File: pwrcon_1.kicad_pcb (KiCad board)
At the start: 2 copper layers, 98.3 x 58.4 mm, 36 parts, among them J1 Conn_01x02, J4 CON3, J5 Conn_01x03_Female, J6 Conn_02x04_Odd_Even, J7 Conn_01x03_Female, Q1 Q_PNP_BCE, U1 LM358

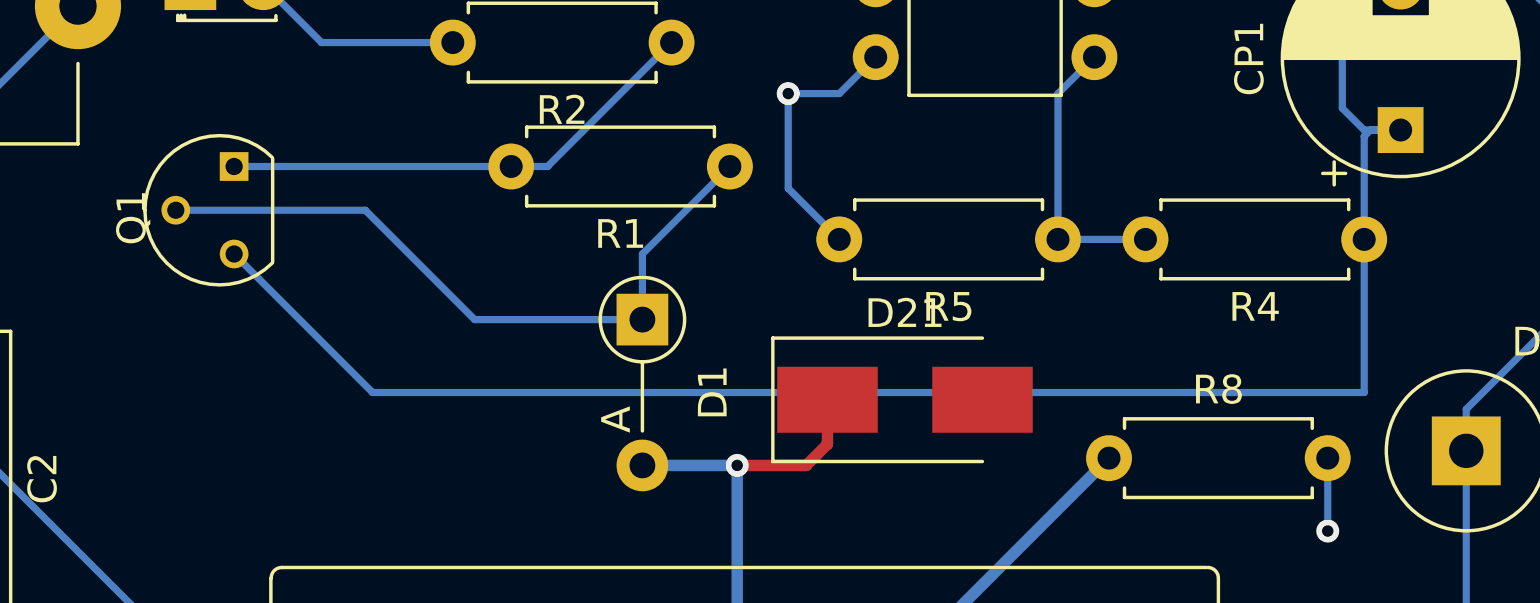
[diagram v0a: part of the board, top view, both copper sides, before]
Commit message: Changed pcb file for transistor flip in previous commit. Changed PSU module name in schematic
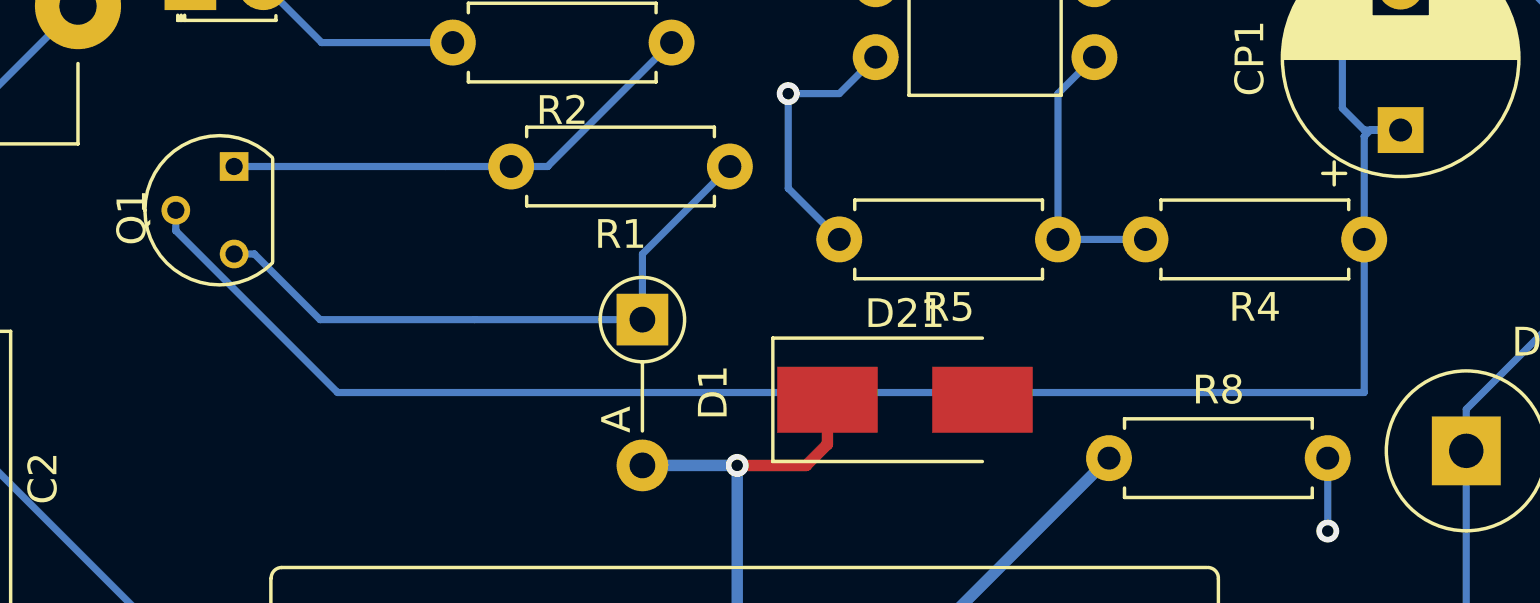
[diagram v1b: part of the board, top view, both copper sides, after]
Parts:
- PSU1: value PD05-20BXX -> IRM-01-3.3
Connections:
- Q1 pad 2: Net-(D1-Pad1) -> Net-(CP1-Pad1)
- Q1 pad 3: Net-(CP1-Pad1) -> Net-(D1-Pad1)
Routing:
- net Net-(CP1-Pad1): track 68.6 -> 71.7 mm
- net Net-(D1-Pad1): track 24.4 -> 21.8 mm
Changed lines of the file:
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@@
-(kicad_pcb (version 20171130) (host pcbnew 5.1.2-f72e74a~84~ubuntu18.04.1)
+(kicad_pcb (version 20171130) (host pcbnew 5.1.5-52549c5~84~ubuntu18.04.1)
   (general
     (thickness 1.6)
     (drawings 8)
-    (tracks 152)
+    (tracks 155)
     (zones 0)
     (modules 36)
@@
   )
   (setup
-    (last_trace_width 0.4)
+    (last_trace_width 0.25)
     (user_trace_width 0.4)
     (user_trace_width 0.5)
@@
       (effects (font (size 1 1) (thickness 0.15)))
     )
-    (fp_text value PD05-20BXX (at -10.16 8.39) (layer F.Fab)
+    (fp_text value IRM-01-3.3 (at -10.16 8.39) (layer F.Fab)
       (effects (font (size 1 1) (thickness 0.15)))
     )
@@
     )
     (pad 3 thru_hole circle (at 0 0 180) (size 1 1) (drill 0.6) (layers *.Cu *.Mask)
-      (net 11 "Net-(CP1-Pad1)"))
+      (net 9 "Net-(D1-Pad1)"))
     (pad 1 thru_hole rect (at 3.048 0 180) (size 1 1) (drill 0.6) (layers *.Cu *.Mask)
       (net 8 "Net-(Q1-Pad1)"))
     (pad 2 thru_hole circle (at 1.524 -2.032 180) (size 1 1) (drill 0.6) (layers *.Cu *.Mask)
-      (net 9 "Net-(D1-Pad1)"))
+      (net 11 "Net-(CP1-Pad1)"))
     (model ${KISYS3DMOD}/TO_SOT_Packages_THT.3dshapes/TO-92_Molded_Narrow.wrl
       (offset (xyz 1.269999980926514 0 0))
@@
   (segment (start 157.48 81.026) (end 161.798 76.708) (width 0.25) (layer B.Cu) (net 8))
   (segment (start 156.21 81.026) (end 157.48 81.026) (width 0.25) (layer B.Cu) (net 8))
-  (segment (start 144.526 82.55) (end 151.13 82.55) (width 0.25) (layer B.Cu) (net 9))
   (segment (start 154.94 86.36) (end 160.782 86.36) (width 0.25) (layer B.Cu) (net 9))
-  (segment (start 151.13 82.55) (end 154.94 86.36) (width 0.25) (layer B.Cu) (net 9))
   (segment (start 160.782 84.074) (end 163.83 81.026) (width 0.25) (layer B.Cu) (net 9))
   (segment (start 160.782 86.36) (end 160.782 84.074) (width 0.25) (layer B.Cu) (net 9))
+  (segment (start 149.551106 86.36) (end 154.94 86.36) (width 0.25) (layer B.Cu) (net 9))
+  (segment (start 147.265106 84.074) (end 149.551106 86.36) (width 0.25) (layer B.Cu) (net 9))
+  (segment (start 146.558 84.074) (end 147.265106 84.074) (width 0.25) (layer B.Cu) (net 9))
   (segment (start 149.606 76.708) (end 154.178 76.708) (width 0.25) (layer B.Cu) (net 10))
   (segment (start 147.574 74.676) (end 149.606 76.708) (width 0.25) (layer B.Cu) (net 10))
@@
   (segment (start 177.329999 70.395999) (end 180.123999 70.395999) (width 0.25) (layer B.Cu) (net 11))
   (segment (start 176.53 69.596) (end 177.329999 70.395999) (width 0.25) (layer B.Cu) (net 11))
-  (segment (start 185.928 88.9) (end 185.928 83.566) (width 0.25) (layer B.Cu) (net 11))
-  (segment (start 146.558 84.074) (end 151.384 88.9) (width 0.25) (layer B.Cu) (net 11))
-  (segment (start 151.384 88.9) (end 185.928 88.9) (width 0.25) (layer B.Cu) (net 11))
+  (segment (start 144.526 83.257106) (end 144.526 82.55) (width 0.25) (layer B.Cu) (net 11))
+  (segment (start 185.928 88.9) (end 150.162998 88.9) (width 0.25) (layer B.Cu) (net 11))
+  (segment (start 144.526 83.263002) (end 144.526 83.257106) (width 0.25) (layer B.Cu) (net 11))
+  (segment (start 150.162998 88.9) (end 144.526 83.263002) (width 0.25) (layer B.Cu) (net 11))
+  (segment (start 185.928 83.566) (end 185.928 88.9) (width 0.25) (layer B.Cu) (net 11))
   (segment (start 181.61 65.278) (end 180.34 65.278) (width 0.25) (layer B.Cu) (net 12))
   (segment (start 184.658 68.326) (end 181.61 65.278) (width 0.25) (layer B.Cu) (net 12))

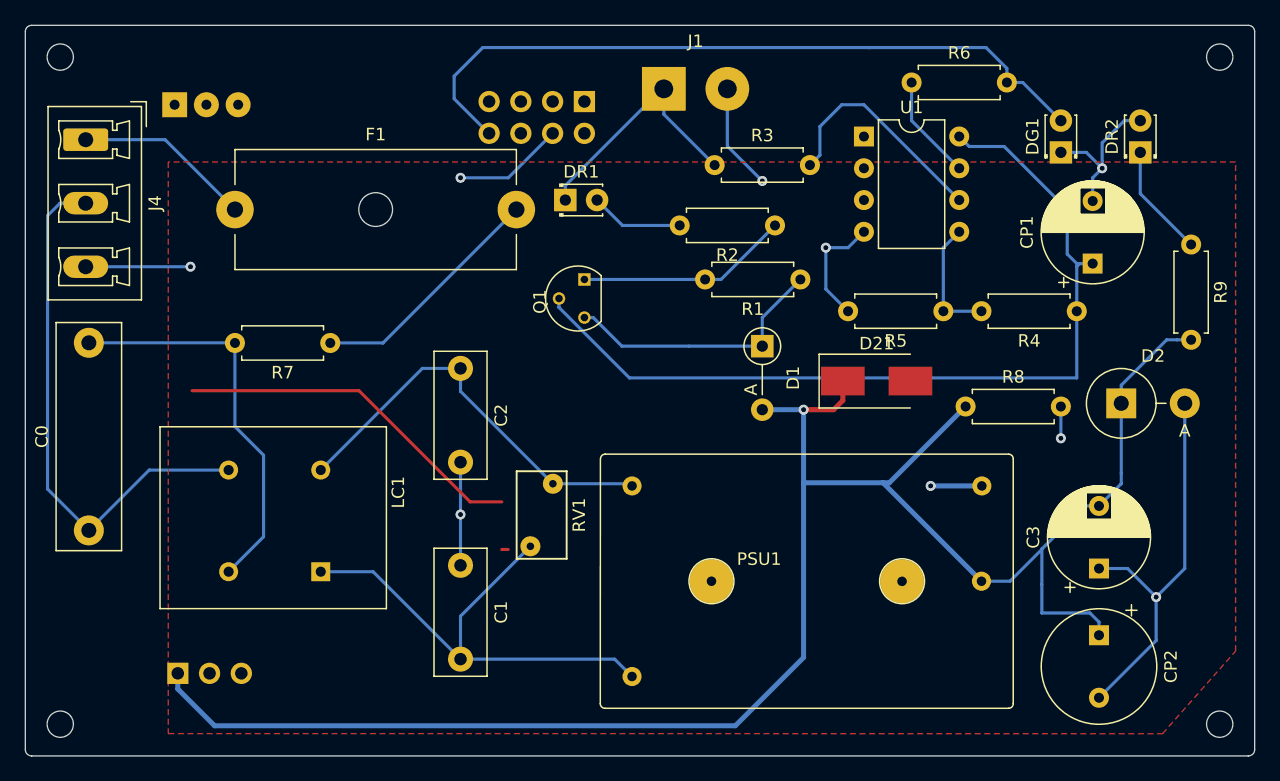
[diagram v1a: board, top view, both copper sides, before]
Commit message: Changed module to 5V, added 3V3 regulator and isolated RS485 transceiver, changed to SMD
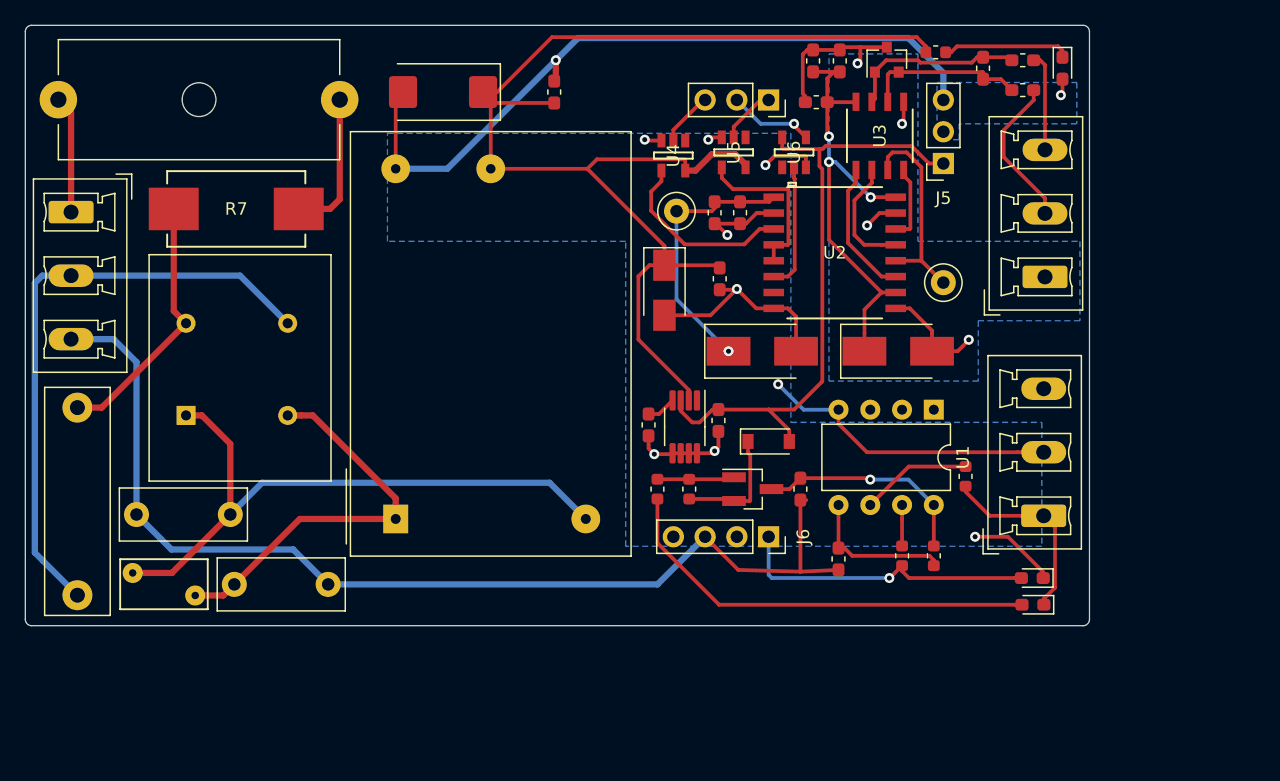
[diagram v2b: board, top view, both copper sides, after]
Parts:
- removed CP1: CP, Capacitor_THT:CP_Radial_D8.0mm_P5.00mm
- removed D21: SMAJ6 0A, Diode_SMD:D_SMB_Handsoldering
- removed PSU1: IRM-01-3.3, pwrcon:Meanwell_IRM_01_fixed
- removed REF** (x4): MountingHole_2.1mm, MountingHole:MountingHole_2.1mm
- added C10: 1u, Capacitor_SMD:C_0603_1608Metric_Pad1.05x0.95mm_HandSolder, F.Cu at (157.3, 92.3)
- added C11: 470p, Capacitor_SMD:C_0603_1608Metric_Pad1.05x0.95mm_HandSolder, F.Cu at (151.7, 92.7)
- added C4: 0.1u, Capacitor_SMD:C_0603_1608Metric_Pad1.05x0.95mm_HandSolder, F.Cu at (167.0, 63.6)
- added C5: 10u, Capacitor_SMD:C_0603_1608Metric_Pad1.05x0.95mm_HandSolder, F.Cu at (164.8, 63.6)
- added C6: 0.1u, Capacitor_SMD:C_0603_1608Metric_Pad1.05x0.95mm_HandSolder, F.Cu at (165.1, 66.9)
- added C7: 10u, Capacitor_SMD:C_0603_1608Metric_Pad1.05x0.95mm_HandSolder, F.Cu at (159.0, 75.7)
- added C8: 0.1u, Capacitor_SMD:C_0603_1608Metric_Pad1.05x0.95mm_HandSolder, F.Cu at (157.0, 75.7)
- added C9: C_Small, Capacitor_SMD:C_0603_1608Metric_Pad1.05x0.95mm_HandSolder, F.Cu at (163.8, 97.8)
- added D4: D_Zener_Small, Diode_SMD:D_SMB_Handsoldering, F.Cu at (171.7, 86.8)
- added D5: D_Zener_Small, Diode_SMD:D_SMB_Handsoldering, F.Cu at (160.8, 86.8)
- added D6: CDSOT23-SM712, Package_TO_SOT_SMD:SOT-23, F.Cu at (170.7, 63.4)
- added J8: Conn_01x03_Female, Connector_PinSocket_2.54mm:PinSocket_1x03_P2.54mm_Vertical, F.Cu at (161.3, 66.7)
- added PS1: IRM-01-5, Converter_ACDC:Converter_ACDC_MeanWell_IRM-02-xx_THT, F.Cu at (131.5, 100.2)
- added R10: 10, Resistor_SMD:R_0603_1608Metric_Pad1.05x0.95mm_HandSolder, F.Cu at (181.6, 63.5)
- added R11: 10, Resistor_SMD:R_0603_1608Metric_Pad1.05x0.95mm_HandSolder, F.Cu at (181.6, 65.9)
- added R12: 120, Resistor_SMD:R_0603_1608Metric_Pad1.05x0.95mm_HandSolder, F.Cu at (178.4, 64.1)
- added TP4: TestPoint, TestPoint:TestPoint_Loop_D2.50mm_Drill1.0mm, F.Cu at (175.3, 81.3)
- added TP7: TestPoint, TestPoint:TestPoint_Loop_D2.50mm_Drill1.0mm, F.Cu at (153.9, 75.6)
- added U2: ISOW7841DWE, ISOW7841DWE:ISOW7841DWE, F.Cu at (166.6, 78.9)
- added U3: THVD1500D, THVD1500D:THVD1500D, F.Cu at (170.2, 69.5)
- added U4: SN74LV1T34DBVR, SN74LV1T34DBVR:SN74LV1T34DBVR, F.Cu at (153.7, 71.1)
- added U5: SN74LV1T34DBVR, SN74LV1T34DBVR:SN74LV1T34DBVR, F.Cu at (158.5, 70.9)
- added U6: SN74LV1T34DBVR, SN74LV1T34DBVR:SN74LV1T34DBVR, F.Cu at (163.3, 70.9)
- added U7: MIC5219-3.3YMM, Package_SO:MSOP-8_3x3mm_P0.65mm, F.Cu at (154.6, 92.8)
- C3: footprint Capacitor_THT:CP_Radial_D8.0mm_P5.00mm -> Capacitor_SMD:C_0603_1608Metric_Pad1.05x0.95mm_HandSolder
- CP2: footprint Capacitor_THT:CP_Radial_Tantal_D9.0mm_P5.00mm -> Capacitor_Tantalum_SMD:CP_EIA-7343-20_Kemet-V_Pad2.25x2.55mm_HandSolder
- D1: footprint Diode_THT:D_A-405_P5.08mm_Vertical_AnodeUp -> Diode_SMD:D_SOD-123
- D2: footprint Diode_THT:D_DO-27_P5.08mm_Vertical_AnodeUp -> Diode_SMD:D_SMA
- DG1, DR1, DR2: footprint LED_THT:LED_D1.8mm_W3.3mm_H2.4mm -> LED_SMD:LED_0603_1608Metric_Pad1.05x0.95mm_HandSolder
- J1: value Conn_01x02 -> CON3; footprint Connector_Wire:SolderWirePad_1x02_P5.08mm_Drill1.5mm -> Connector_Phoenix_MC_HighVoltage:PhoenixContact_MCV_1,5_3-G-5.08_1x03_P5.08mm_Vertical
- J5: moved to F.Cu
- J6: value Conn_02x04_Odd_Even -> Conn_01x04; footprint Connector_PinSocket_2.54mm:PinSocket_2x04_P2.54mm_Vertical -> Connector_PinSocket_2.54mm:PinSocket_1x04_P2.54mm_Vertical; moved to F.Cu
- J7: value Conn_01x03_Female -> CON3; footprint pwrcon:SolderWirePad_1x03_P2.54mm_Drill0.8mm -> Connector_Phoenix_MC_HighVoltage:PhoenixContact_MCV_1,5_3-G-5.08_1x03_P5.08mm_Vertical; moved to F.Cu
- Q1: value Q_PNP_BCE -> Q_PNP_BEC; footprint pwrcon:TO-92_BC237_307 -> Package_TO_SOT_SMD:SOT-23_Handsoldering
- R1, R2, R3, R4, R6, R9: footprint Resistor_THT:R_Axial_DIN0207_L6.3mm_D2.5mm_P7.62mm_Horizontal -> Resistor_SMD:R_0603_1608Metric
- R5, R8: footprint Resistor_THT:R_Axial_DIN0207_L6.3mm_D2.5mm_P7.62mm_Horizontal -> Resistor_SMD:R_0603_1608Metric_Pad1.05x0.95mm_HandSolder
- R7: value 10R 3W -> SMW310RJT; footprint Resistor_THT:R_Axial_DIN0207_L6.3mm_D2.5mm_P7.62mm_Horizontal -> SMW310RJT:SMW310RJT
- moved J5 73.5 mm to (175.3, 71.8), turned to 180 degrees
- moved J7 70.9 mm to (183.4, 80.8), turned to 90 degrees
- moved CP2 68.1 mm to (135.3, 66.0), turned to 180 degrees
- moved C3 57.9 mm to (144.1, 66.0), turned to 270 degrees
- moved DR1 49.4 mm to (182.4, 107.0), turned to 180 degrees
- moved J1 45.7 mm to (183.3, 99.9), turned to 90 degrees
- moved R6 37.9 mm to (172.0, 103.1), turned to 270 degrees
- moved J6 37.8 mm to (161.3, 101.6), turned to 270 degrees
- moved D2 37.6 mm to (153.0, 81.9), turned to 270 degrees
- moved DG1 34.1 mm to (182.4, 104.9), turned to 180 degrees
- moved R3 32.0 mm to (177.0, 96.8), turned to 90 degrees
- moved RV1 31.9 mm to (110.4, 104.5), turned to 0 degrees
- moved C1 26.2 mm to (110.7, 99.8), turned to 0 degrees
- moved R9 25.6 mm to (174.7, 62.9), turned to 180 degrees
- moved C2 25.0 mm to (118.6, 105.4), turned to 0 degrees
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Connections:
- net Net-(DR1-Pad1) renamed /NC
- net Net-(Q1-Pad1) renamed /Q1B
- C3 pad 2: /ACDC_OUT3_3V -> /5VDC
- CP2 pad 1: /ACDC_OUT3_3V -> /5VDC
- D1 pad 1: Net-(D1-Pad1) -> /Q1E
- D1 pad 2: /ACDC_OUT3_3V -> /3V3
- D2 pad 1: /ACDC_OUT3_3V -> /5VDC
- J5 pad 1: /ACDC_OUT3_3V -> /3V3
- J6 pad 1: (no net) -> Net-(DG1-Pad2)
- J6 pad 3: (no net) -> GND
- J6 pad 4: GND -> (no net)
- J7 pad 1: (no net) -> GNDA
- J7 pad 2: (no net) -> Net-(J7-Pad2)
- J7 pad 3: (no net) -> Net-(J7-Pad3)
- Q1 pad 2: Net-(CP1-Pad1) -> /Q1E
- Q1 pad 3: Net-(D1-Pad1) -> Net-(C9-Pad2)
- R1 pad 1: Net-(D1-Pad1) -> /Q1E
- R4 pad 1: Net-(CP1-Pad1) -> Net-(C9-Pad2)
- R7 pad 1: Net-(F1-Pad2) -> Net-(C0-Pad2)
- R7 pad 2: Net-(C0-Pad2) -> Net-(F1-Pad2)
- R8 pad 1: /ACDC_OUT3_3V -> /5VDC
- R9 pad 2: /ACDC_OUT3_3V -> /5VDC
- U1 pad 8: Net-(CP1-Pad1) -> Net-(C9-Pad2)
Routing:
- net /ACDC_OUT3_3V: track 149.9 -> 0.00 mm, vias 1 -> 0
- net /5VDC: track 0.00 -> 101.9 mm
- net GND: track 124.3 -> 215.8 mm, vias 9 -> 11
- net Net-(CP1-Pad1): track 71.7 -> 0.00 mm
- net /3V3: track 0.00 -> 50.2 mm
- net Net-(C4-Pad2): track 0.00 -> 37.5 mm, vias 0 -> 3
- net Net-(DG1-Pad2): track 58.5 -> 24.4 mm, vias 0 -> 1
- net Net-(DR1-Pad2): track 7.45 -> 34.7 mm
- net GNDA: track 0.00 -> 25.4 mm, vias 0 -> 4
- net Net-(C7-Pad1): track 0.00 -> 22.5 mm, vias 0 -> 1
- net Net-(D1-Pad1): track 21.8 -> 0.00 mm
- net Net-(C9-Pad2): track 0.00 -> 17.5 mm, vias 0 -> 1
- net Net-(TP4-Pad1): track 0.00 -> 16.4 mm
- net Net-(U2-Pad3): track 0.00 -> 15.6 mm
- net Net-(D6-Pad1): track 0.00 -> 14.2 mm
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- added copper zone on B.Cu, net GND
- added copper zone on B.Cu, net GNDA
- removed copper zone on F.Cu, net GND
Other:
- board size 98.3 x 58.4 mm -> 85.1 x 48 mm

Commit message: Preliminary routing
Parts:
- removed TP7: TestPoint, TestPoint:TestPoint_Loop_D2.50mm_Drill1.0mm
- TP4: footprint TestPoint:TestPoint_Loop_D2.50mm_Drill1.0mm -> TestPoint:TestPoint_Loop_D1.80mm_Drill1.0mm_Beaded
- moved C10 15.0 mm to (156.8, 77.3)
- moved C11 15.0 mm to (151.2, 77.7)
- moved U7 15.0 mm to (154.1, 77.8)
- moved D2 3.71 mm to (152.9, 85.6)
- moved C8 2.05 mm to (159.0, 75.9)
- moved R8 1.82 mm to (156.5, 82.5)
- moved C7 1.80 mm to (160.8, 75.9)
- moved TP4 1.37 mm to (176.5, 80.8), turned to 0 degrees
- moved U2 1.32 mm to (167.9, 78.9)
- moved U6 0.76 mm to (162.6, 70.9)
- moved U3 0.51 mm to (169.7, 69.5)
- moved D5 0.10 mm to (160.8, 86.9)
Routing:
- net /5VDC: track 101.9 -> 79.6 mm
- net Net-(C7-Pad1): track 22.5 -> 17.2 mm, vias 1 -> 0
- net GND: track 215.8 -> 212.0 mm
- net /3V3: track 50.2 -> 53.7 mm
- net Net-(TP4-Pad1): track 16.4 -> 18.6 mm
- net Net-(U2-Pad6): track 10.1 -> 12.3 mm
- net Net-(U2-Pad14): track 6.09 -> 8.17 mm
- net Net-(U2-Pad3): track 15.6 -> 13.9 mm, vias 0 -> 2
- net Net-(U2-Pad13): track 9.41 -> 8.19 mm
- net Net-(C4-Pad2): track 37.5 -> 38.3 mm
- net Net-(U2-Pad11): track 11.0 -> 11.8 mm
- net Net-(D6-Pad1): track 14.2 -> 14.8 mm
- net /RS485_RXD: track 6.84 -> 6.23 mm
- net GNDA: track 25.4 -> 24.9 mm
- net Net-(U2-Pad4): track 13.4 -> 13.3 mm, vias 0 -> 2
- added copper zone on F.Cu, net /5VDC
